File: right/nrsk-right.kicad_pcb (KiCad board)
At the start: 2 copper layers, 187 x 120.3 mm, 133 parts, among them J1 PJ-320D, J2 USB-C, J3 OLED 128x32, SW1 71, SW10 8, SW11 9, SW12 0, SW13 -, SW14 =, SW15 Backspace, SW16 75, SW17 Y, SW18 U, SW19 I, SW2 F7, SW20 O, SW21 P, SW22 [, SW23 ], SW24 \, SW25 77, SW26 H, SW27 J, SW28 K, SW29 L, SW3 F8, SW30 ;, SW31 ', SW32 Enter, SW33 79, SW34 N, SW35 M, SW36 ,, SW37 ., SW38 /, SW39 ↑, SW4 F9, SW40 fn, SW41 81, SW42 Space, SW43 Space, SW44 Cmd, SW45 Opt, SW46 ←, SW47 ↓, SW48 →, SW5 F10, SW6 F11, SW7 F12, SW8 73, SW9 7, U1 ATmega32U4-AU, U2 USBLC6-2SC6, U3 AS5600-ASOM, Y1 16MHz

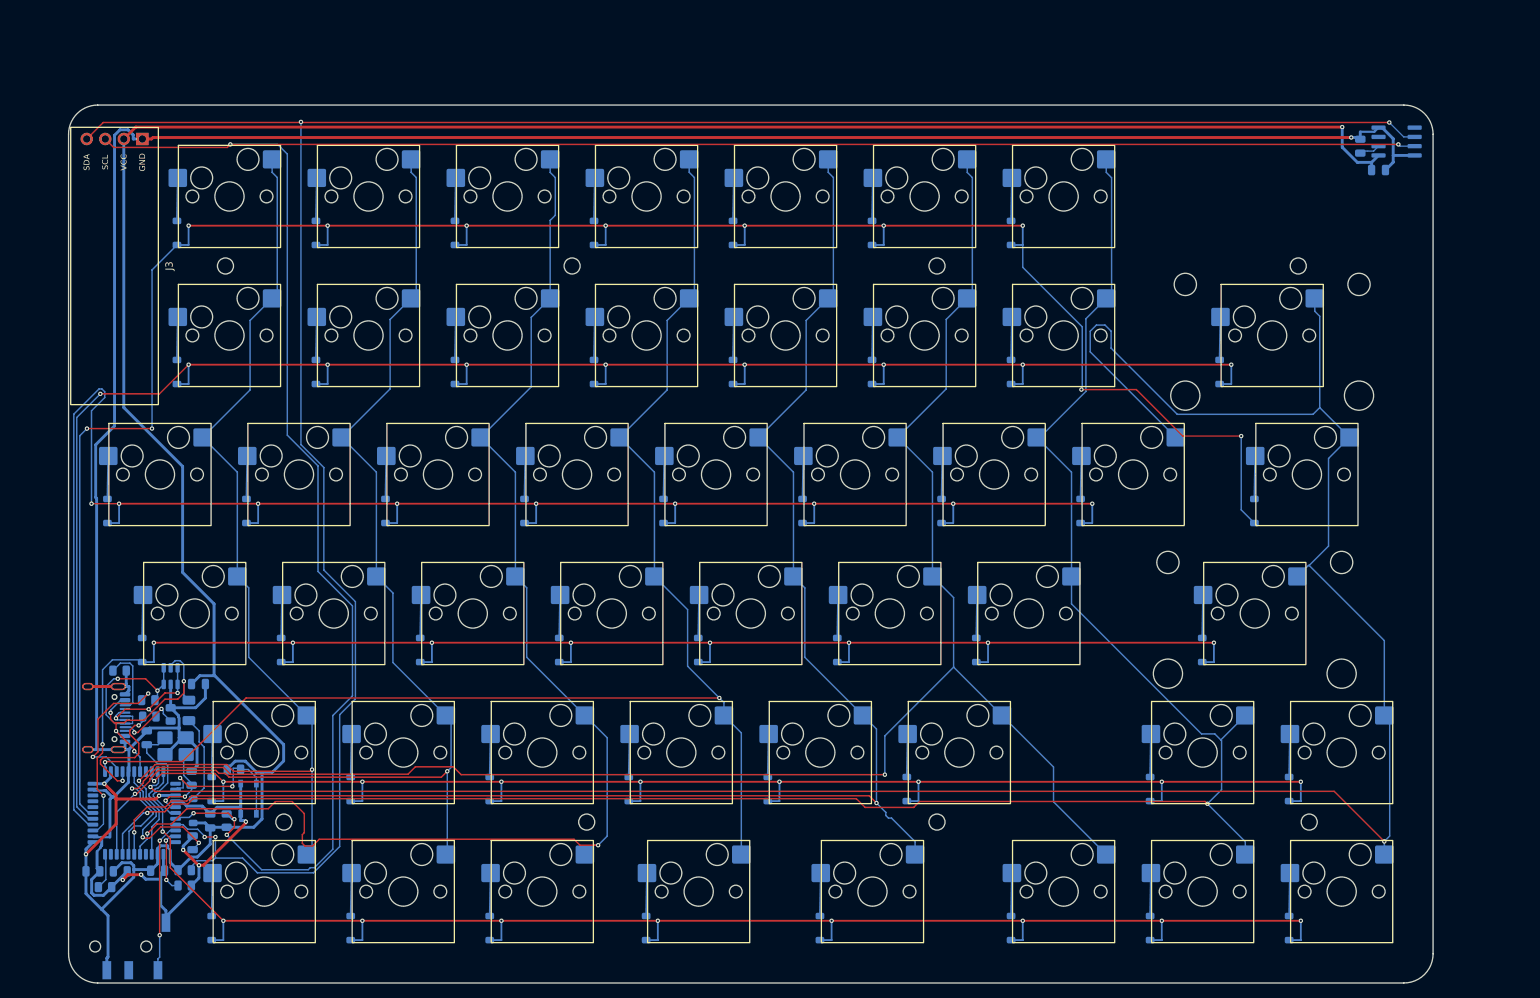
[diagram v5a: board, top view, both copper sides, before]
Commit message: Move to RP2040, rework OLED/connectors/wheel, add all-printed case and assembly guide
- MCU: RP2040 + W25Q128JV + 12 MHz crystal + AP2112K 3.3 V LDO on each half;
  QMK config for RP2040 (UF2, PIO serial, I2C1 on GP2/GP3); routing helped by
  MCU escape stubs, TESTEN-to-pad stub, exposed-pad vias and a fan-out ring
- Boards: top edge +5 mm, inner edges widened; USB-C on the back edge, TRRS
  behind the OLED at the same height on both halves
- OLED: half-mirror acrylic (2 mm) rounded rectangle centred on the display,
  flush with the plate, held by double-sided tape
- Wheel: 32 rim teeth + M3 ball plunger for detents; removable corner cap so
  the printed tray can be assembled; magnet shown in viewer
- Case variants: A (printed tray + clear acrylic plate), B (all printed, plate
  with stiffening web), acrylic stack; slim-head M2 plate screws; tray fillets
- Viewer: shared model-data.js, wheel toggle, rotate below; new interactive
  assembly guide (case/preview/assembly.html, also on Pages)
- BOM: RP2040 parts, plunger, slim-head screws, acrylic finishes, all with
  verified sources; README and renders updated

Co-Authored-By: Claude Opus 5.5 <noreply@anthropic.com>
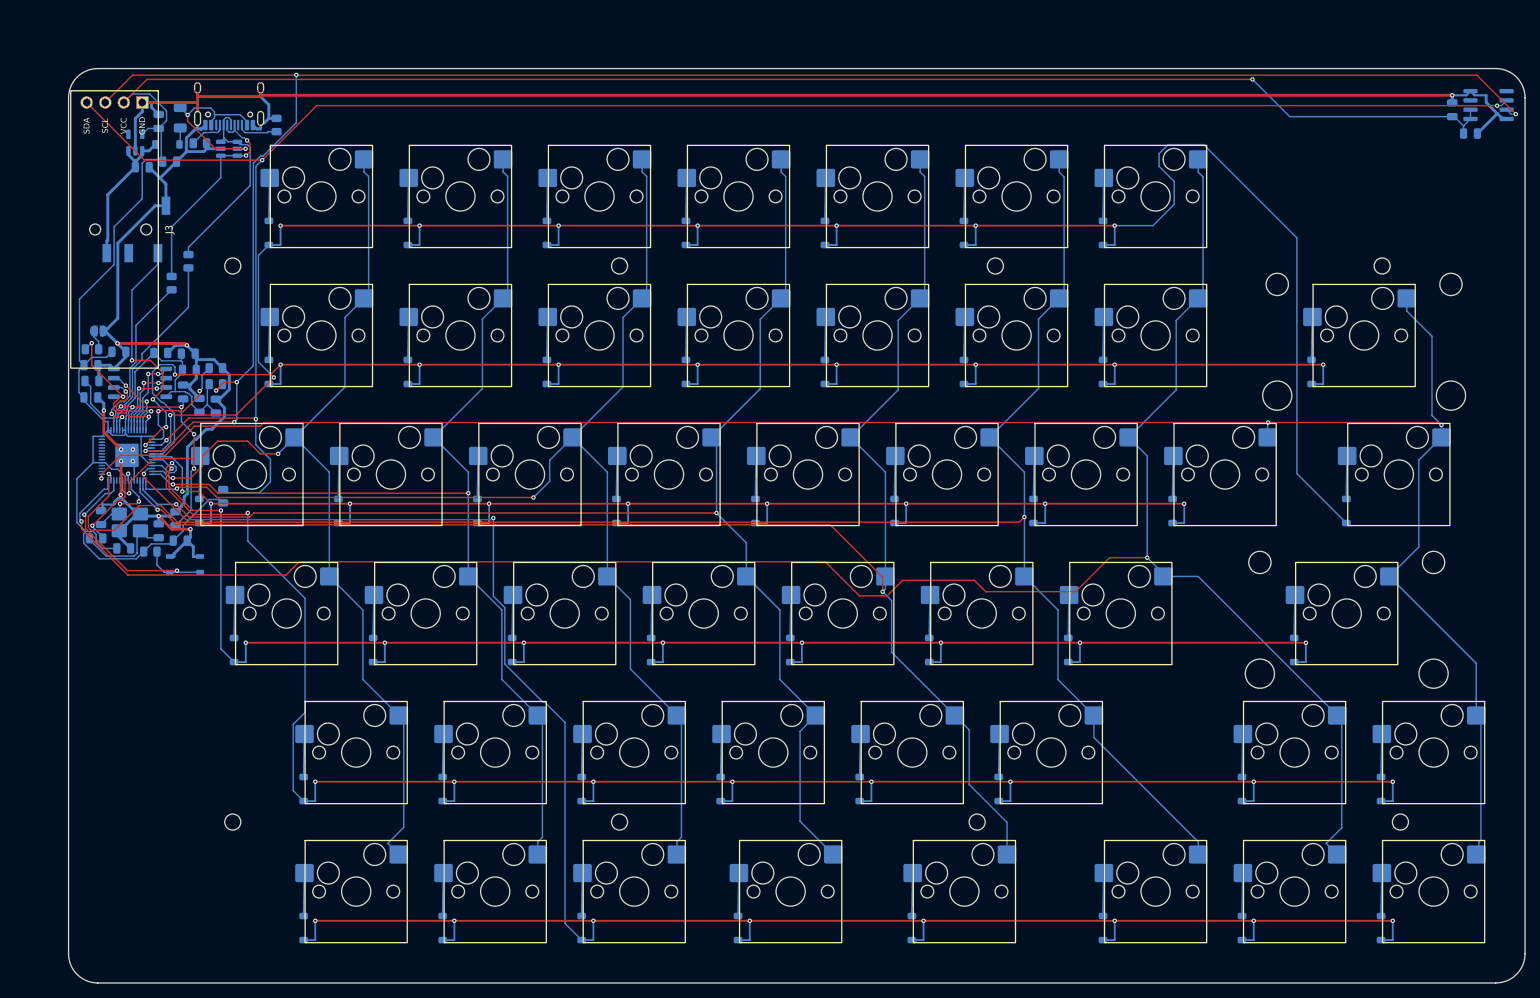
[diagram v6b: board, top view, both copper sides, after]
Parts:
- added C11: 0.1uF, Capacitor_SMD:C_0805_2012Metric, B.Cu at (42.3, 86.7)
- added C12: 0.1uF, Capacitor_SMD:C_0805_2012Metric, B.Cu at (34.6, 87.8)
- added C13: 0.1uF, Capacitor_SMD:C_0805_2012Metric, B.Cu at (30.1, 62.6)
- added C14: 0.1uF, Capacitor_SMD:C_0805_2012Metric, B.Cu at (43.5, 63.3)
- added C15: 0.1uF, Capacitor_SMD:C_0805_2012Metric, B.Cu at (43.4, 61.1)
- added C16: 1uF, Capacitor_SMD:C_0805_2012Metric, B.Cu at (37.1, 35.5)
- added C17: 1uF, Capacitor_SMD:C_0805_2012Metric, B.Cu at (39.4, 29.3)
- added C18: 0.1uF, Capacitor_SMD:C_0805_2012Metric, B.Cu at (33.9, 60.8)
- added C19: 10uF, Capacitor_SMD:C_0805_2012Metric, B.Cu at (40.9, 34.8)
- added C20: 0.1uF, Capacitor_SMD:C_0805_2012Metric, B.Cu at (39.6, 61.0)
- added JP1: BOOTSEL, Jumper:SolderJumper-2_P1.3mm_Open_RoundedPad1.0x1.5mm, B.Cu at (31.1, 58.0)
- added R10: 1k, Resistor_SMD:R_0805_2012Metric, B.Cu at (30.8, 86.4)
- added U4: AP2112K-3.3, Package_TO_SOT_SMD:SOT-23-5, B.Cu at (36.1, 32.1)
- added U5: W25Q128JVS, Package_SO:SOIC-8_5.3x5.3mm_P1.27mm, B.Cu at (36.8, 65.1)
- C1, C2: value 22pF -> 15pF
- C4: value 0.1uF -> 1uF
- C8: value 10uF -> 0.1uF
- R2, R3: value 22 -> 27
- R7: value 10k -> 1k
- U1: value ATmega32U4-AU -> RP2040; footprint Package_QFP:TQFP-44_10x10mm_P0.8mm -> Package_DFN_QFN:QFN-56-1EP_7x7mm_P0.4mm_EP3.2x3.2mm
- Y1: value 16MHz -> 12MHz
- moved J1 98.3 mm to (35.4, 44.0)
- moved D99 91.4 mm to (40.5, 32.4), turned to 0 degrees
- moved J2 87.2 mm to (49.0, 25.7), turned to 0 degrees
- moved F1 81.2 mm to (42.3, 28.7)
- moved R4 78.4 mm to (45.0, 32.2), turned to 0 degrees
- moved R5 77.8 mm to (55.5, 29.7), turned to 90 degrees
- moved R7 73.7 mm to (30.2, 60.5)
- moved U2 72.7 mm to (49.0, 33.0), turned to 0 degrees
- moved R1 71.0 mm to (47.2, 63.0)
- moved C6 65.7 mm to (42.7, 66.3), turned to 90 degrees
- moved C7 65.5 mm to (44.9, 68.2), turned to 90 degrees
- moved C8 65.1 mm to (47.2, 68.2), turned to 90 degrees
- moved C3 62.6 mm to (30.1, 67.1), turned to 0 degrees
- moved R3 60.4 mm to (43.4, 48.4), turned to 90 degrees
- moved R8 59.8 mm to (47.2, 65.2), turned to 0 degrees
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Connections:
- C1 pad 1: /XTAL1 -> /XIN
- C10 pad 1: VCC -> /3V3
- C2 pad 1: /XTAL2 -> /XTAL
- C3 pad 1: /UCAP -> /3V3
- C4 pad 1: VCC -> /1V1
- C5 pad 1: VCC -> /1V1
- C6 pad 1: VCC -> /1V1
- C7 pad 1: VCC -> /3V3
- C8 pad 1: VCC -> /3V3
- C9 pad 1: /VDD3V3 -> /3V3
- J3 pad 2: VCC -> /3V3
- R6 pad 1: VCC -> /3V3
- R6 pad 2: /RST -> /RUN
- R7 pad 1: /HWB -> /QSPI_SS
- R7 pad 2: GND -> /BOOT
- R8 pad 1: VCC -> /3V3
- R9 pad 1: VCC -> /3V3
- RSW1 pad 1: /RST -> /RUN
- U1 pad 1: /COL3 -> /3V3
- U1 pad 10: /COL7 -> /3V3
- U1 pad 11: /ROW5 -> /ROW4
- U1 pad 12: unconnected-(U1-PB7-Pad12) -> /ROW5
- U1 pad 13: /RST -> /COL0
- U1 pad 14: VCC -> /COL1
- U1 pad 15: GND -> /COL2
- U1 pad 16: /XTAL2 -> /COL3
- U1 pad 17: /XTAL1 -> /COL4
- U1 pad 18: /SCL -> unconnected-(U1-GPIO15-Pad18)
- U1 pad 19: /SDA -> GND
- U1 pad 2: VCC -> /HAND
- U1 pad 20: /DATA -> /XIN
- U1 pad 21: /HAND -> /XOUT
- U1 pad 22: unconnected-(U1-PD5-Pad22) -> /3V3
- U1 pad 23: GND -> /1V1
- U1 pad 24: VCC -> unconnected-(U1-SWCLK-Pad24)
- U1 pad 25: /COL0 -> unconnected-(U1-SWDIO-Pad25)
- U1 pad 26: unconnected-(U1-PD6-Pad26) -> /RUN
- U1 pad 27: /COL2 -> /COL5
- U1 pad 28: /COL4 -> /COL6
- U1 pad 29: /COL5 -> /COL7
- U1 pad 3: /D- -> /DATA
- U1 pad 30: /COL6 -> unconnected-(U1-GPIO19-Pad30)
- U1 pad 31: /COL1 -> unconnected-(U1-GPIO20-Pad31)
- U1 pad 33: /HWB -> /3V3
- U1 pad 34: VCC -> unconnected-(U1-GPIO22-Pad34)
- U1 pad 35: GND -> unconnected-(U1-GPIO23-Pad35)
- U1 pad 36: /ROW3 -> unconnected-(U1-GPIO24-Pad36)
- U1 pad 37: /ROW2 -> unconnected-(U1-GPIO25-Pad37)
- U1 pad 38: /ROW1 -> unconnected-(U1-GPIO26/ADC0-Pad38)
- U1 pad 39: /ROW0 -> unconnected-(U1-GPIO27/ADC1-Pad39)
- U1 pad 4: /D+ -> /SDA
- U1 pad 42: unconnected-(U1-AREF-Pad42) -> /3V3
- U1 pad 43: GND -> /3V3
- U1 pad 44: VCC -> /3V3
- U1 pad 5: GND -> /SCL
- U1 pad 6: /UCAP -> /ROW0
- U1 pad 7: /VBUS -> /ROW1
- U1 pad 8: unconnected-(U1-PB0-Pad8) -> /ROW2
- U1 pad 9: /ROW4 -> /ROW3
- U3 pad 1: VCC -> /3V3
- U3 pad 2: /VDD3V3 -> /3V3
- Y1 pad 1: /XTAL1 -> /XIN
- Y1 pad 3: /XTAL2 -> /XTAL
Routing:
- net /3V3: track 0.00 -> 360.0 mm, vias 0 -> 1
- net VCC: track 375.6 -> 20.1 mm, vias 4 -> 0
- net /ROW5: track 207.4 -> 297.0 mm, vias 9 -> 10
- net /ROW2: track 250.7 -> 180.0 mm
- net /1V1: track 0.00 -> 56.2 mm, vias 0 -> 6
- net /ROW4: track 193.5 -> 247.3 mm, vias 9 -> 10
- net /SDA: track 319.8 -> 269.6 mm
- net /SCL: track 318.9 -> 269.3 mm, vias 5 -> 6
- net /COL7: track 320.7 -> 276.5 mm, vias 2 -> 3
- net /ROW1: track 251.4 -> 211.3 mm
- net /RUN: track 0.00 -> 32.1 mm, vias 0 -> 2
- net GND: track 411.5 -> 381.7 mm, vias 6 -> 11
- net /ROW0: track 294.1 -> 270.5 mm, vias 11 -> 9
- net /UCAP: track 21.6 -> 0.00 mm, vias 2 -> 0
- net /RST: track 21.5 -> 0.00 mm, vias 2 -> 0
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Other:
- board size 187 x 120.3 mm -> 199.6 x 125.3 mm

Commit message: Connector tongues: USB-C / TRRS mouths at the case surface, outline-fit openings
- PCB outline grows a 12 mm tongue under each connector into the case wall;
  the connector mouth sits 0.8 mm inside the outer surface (gen/make_pcb.py)
- Case: openings are just the connector outline + 0.2 mm (rounded slot for
  USB-C, round hole for TRRS); printed tray gets removable port caps over
  the tongues, acrylic frames are notched (gen/make_case.py)
- Port-opening study renders (gen/port_variants.py, docs/img/ports-compare.jpg)
- Viewer, assembly guide (port cap step), BOM, README and images updated

Co-Authored-By: Claude Opus 5.5 <noreply@anthropic.com>
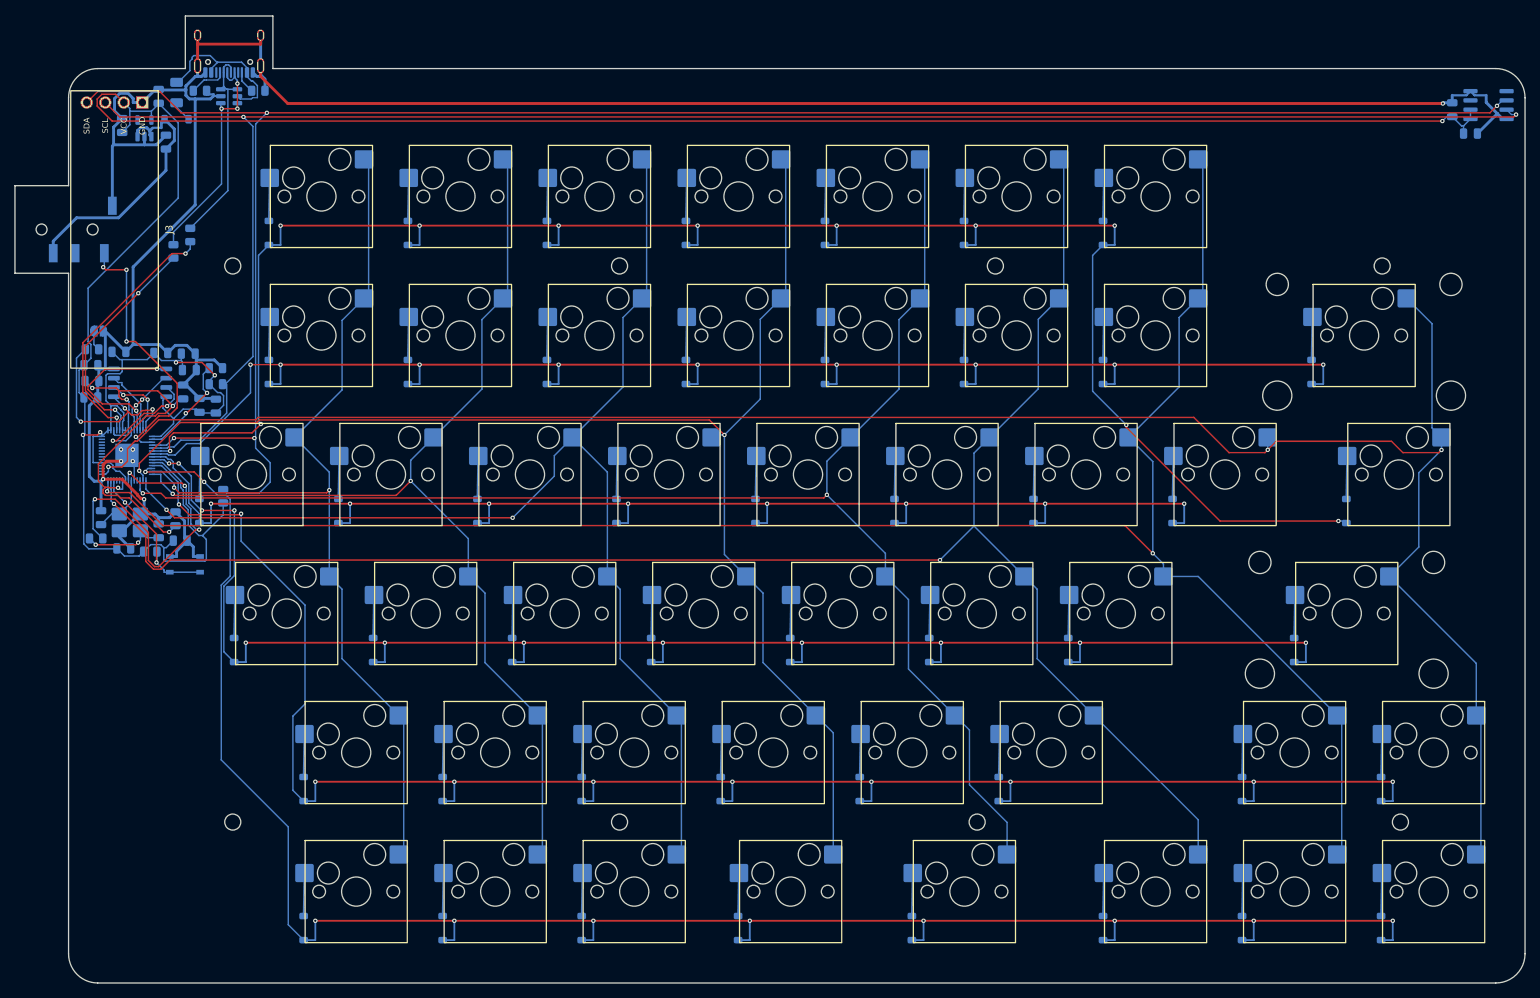
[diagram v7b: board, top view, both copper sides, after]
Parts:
- moved C19 8.17 mm to (34.4, 29.8), turned to 90 degrees
- moved J1 7.35 mm to (28.1, 44.0)
- moved R4 7.20 mm to (45.0, 25.0)
- moved U2 7.20 mm to (49.0, 25.8)
- moved J2 7.20 mm to (49.0, 18.5)
- moved R5 5.32 mm to (53.0, 25.0), turned to 0 degrees
- moved C16 4.74 mm to (40.4, 32.1), turned to 90 degrees
- moved R2 4.36 mm to (41.4, 47.1)
- moved D99 3.67 mm to (41.8, 28.9)
- moved R3 3.61 mm to (43.7, 44.8)
- moved F1 3.49 mm to (41.8, 25.3)
- moved C17 3.45 mm to (39.4, 25.8)
- moved U4 2.32 mm to (37.4, 30.2)
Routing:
- net /ROW5: track 297.0 -> 261.6 mm
- net /3V3: track 360.0 -> 394.8 mm, vias 1 -> 5
- net /XOUT: track 12.7 -> 44.9 mm, vias 2 -> 4
- net /ROW0: track 270.5 -> 250.1 mm, vias 9 -> 11
- net /SCL: track 269.3 -> 251.2 mm, vias 6 -> 2
- net /COL6: track 279.6 -> 263.2 mm
- net VCC: track 20.1 -> 36.0 mm
- net GND: track 381.7 -> 395.8 mm, vias 11 -> 7
- net /COL4: track 219.1 -> 207.4 mm
- net /QSPI_SD0: track 11.1 -> 22.7 mm
- net /RUN: track 32.1 -> 21.9 mm
- net /COL5: track 252.2 -> 242.8 mm
- net /ROW1: track 211.3 -> 201.9 mm
- net /D-: track 26.3 -> 35.6 mm, vias 0 -> 2
- net /D+: track 24.4 -> 31.5 mm
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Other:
- board size 199.6 x 125.3 mm -> 206.9 x 132.5 mm

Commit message: TRRS on the top edge next to USB-C; rounded tongues; B lid fillet; keycap legends
- Both connectors on the back edge (TRRS 17 mm from the inner edge, USB-C 18 mm further out); boards re-routed
- Tongue tips R2.5, roots R1.5 on Edge.Cuts
- Shared port cap when the two ports sit close together
- All-printed plate: R1 on the top outer edge
- Blender renders: keycap legends; refreshed A/B, ports and wheel images

Co-Authored-By: Claude Opus 5.5 <noreply@anthropic.com>
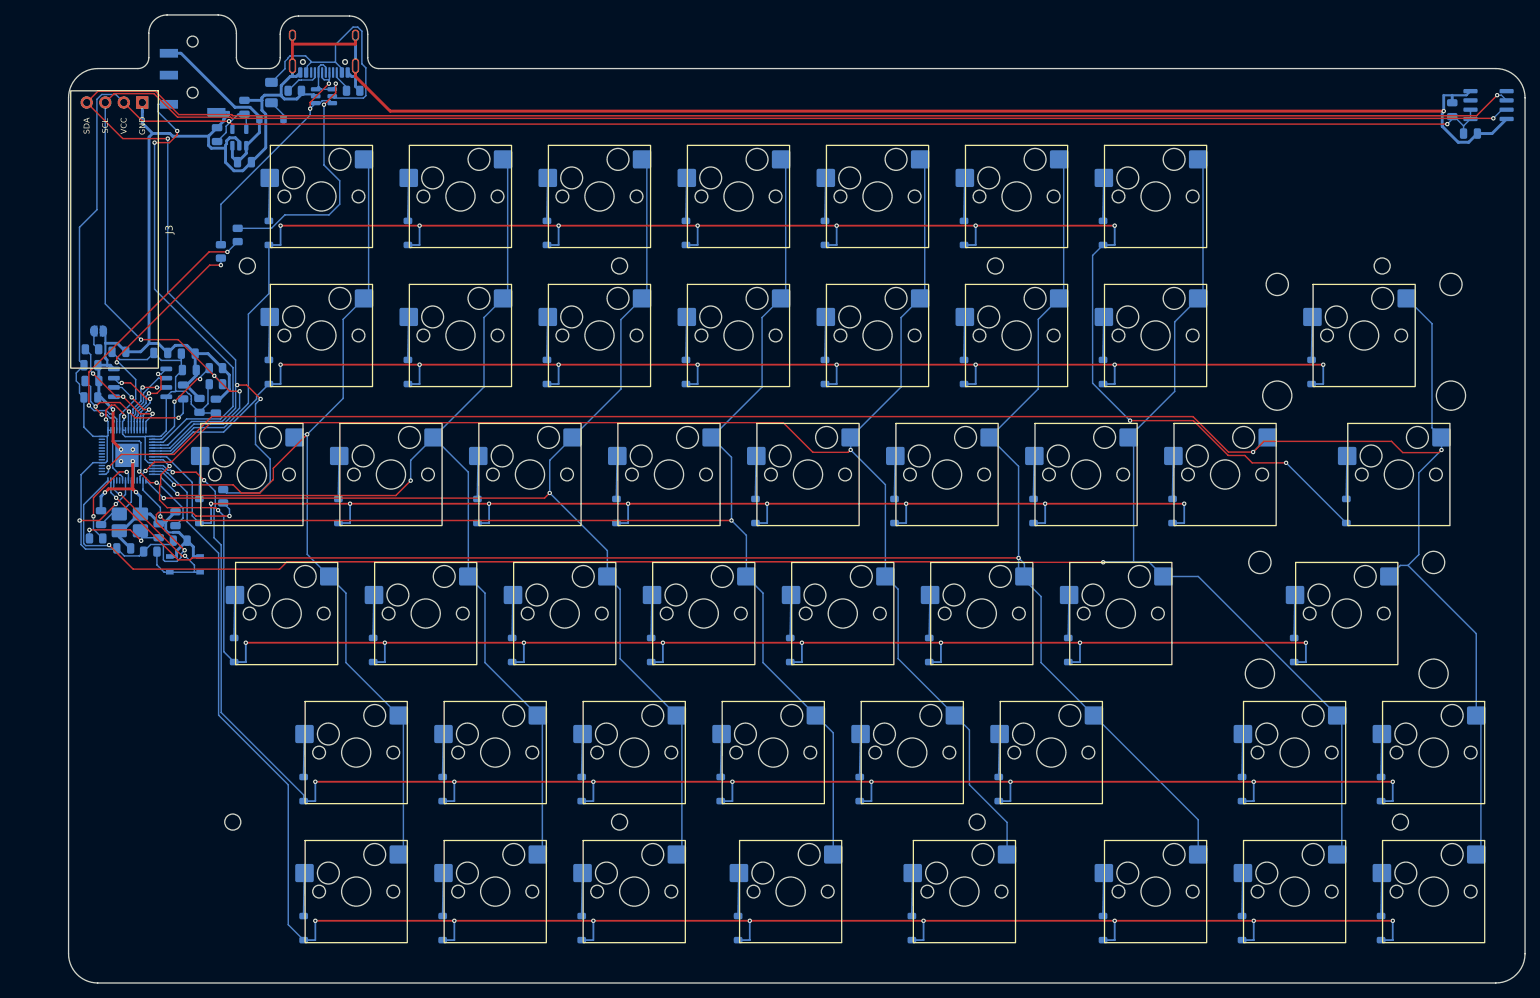
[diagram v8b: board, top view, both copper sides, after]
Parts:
- moved J1 26.3 mm to (44.0, 23.1), turned to -90 degrees
- moved C19 13.1 mm to (47.4, 31.1)
- moved U4 13.1 mm to (50.4, 31.4)
- moved D99 13.0 mm to (54.8, 28.9)
- moved F1 13.0 mm to (54.8, 25.3)
- moved J2 13.0 mm to (62.0, 18.5)
- moved R4 13.0 mm to (58.0, 25.0)
- moved R5 13.0 mm to (66.0, 25.0)
- moved U2 13.0 mm to (62.0, 25.8)
- moved C17 11.8 mm to (51.1, 27.3)
- moved C16 11.1 mm to (51.1, 34.8), turned to 0 degrees
- moved R2 6.50 mm to (47.9, 47.1)
- moved R3 6.50 mm to (50.2, 44.8)
- moved H1 2.00 mm to (51.5, 49.0)
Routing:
- net /XOUT: track 44.9 -> 13.4 mm, vias 4 -> 2
- net /DATA: track 37.7 -> 64.1 mm, vias 4 -> 2
- net /3V3: track 394.8 -> 375.2 mm, vias 5 -> 8
- net /SDA: track 271.0 -> 289.6 mm
- net /VBUS: track 22.3 -> 36.0 mm
- net /USB_D-: track 28.4 -> 41.6 mm, vias 0 -> 2
- net /SCL: track 251.2 -> 263.6 mm, vias 2 -> 4
- net /QSPI_SD0: track 22.7 -> 11.3 mm
- net GND: track 395.8 -> 384.9 mm, vias 7 -> 8
- net VCC: track 36.0 -> 26.0 mm
- net /QSPI_SS: track 27.7 -> 18.1 mm
- net /COL6: track 263.2 -> 272.0 mm
- net /COL2: track 173.6 -> 165.4 mm
- net /QSPI_SD3: track 16.4 -> 9.74 mm
- net /1V1: track 59.0 -> 53.1 mm, vias 5 -> 6
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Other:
- board size 206.9 x 132.5 mm -> 199.6 x 132.6 mm
